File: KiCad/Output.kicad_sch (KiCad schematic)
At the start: 649 parts, among them J1 R_Phono_In, J10 VCC_IN, J11 VCC_OUT, J12 EMK_In, J15 Mic_Effekt_Out, J16 Mic_Effekt_Out, J17 Mic_Effekt_Out, J18 Mic_Effekt_Out, J19 Phono/Line_Out, J2 L_Phono_In, J20 Mic_Effekt_Out, J21 Conn_01x05_bridged, J22 Conn_02x07_Odd_Even, J24 Mic_Effekt_In, J25 Mic_Effekt_In, J26 Phono/Line_In, J27 Mic_Effekt_In, J28 Pegel_Out, J29 Pegel_Out, J3 R_Line_In, J30 Pegel_In, J31 Pegel_In, J32 Pegel_In, J33 Pegel_In, J34 LED_Out, J35 LED_In, J36 VU_Meter_Out, J37 AUX_Send_3, J38 AUX_Send_1, J39 AUX_Send_2, J4 L_Line_In, J40 Bass_Out, J41 Kick_Out, J42 Mid_Out, J43 High_Out, J44 Line_Out_L, J45 Line_Out_R, J5 Mic_In, J6 Effekt_In, J7 AUX_RET_1, J8 AUX_RET_2, J9 AUX_RET_3, SW1 SW_DPST, SW10 SW_SPDT, SW11 SW_SPDT, SW12 SW_SPDT, SW2 SW_SPDT, SW3 SW_SPDT, SW4 SW_SPDT, SW5 SW_SPDT, SW6 SW_SPDT, SW7 SW_SPDT, SW8 SW_SPDT, SW9 SW_Rotary_1x4, U1 TL074, U10 TL074, U11 TL074, U12 TL074, U13 TL074, U14 TL074, U15 TL074, U16 TL074, U17 TL074, U18 TL074, U19 TL074, U2 TL074, U20 TL074, U21 TL074, U22 TL074, U23 TL074, U24 TL074, U25 INA128U, U3 TL074, U4 TL074, U5 TL074, U6 REC10K-2409, U7 REC10K-2415, U8 TL074, U9 TL074

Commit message: final PCB Update
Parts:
- removed C114, C116, C117, C118, C7, C8: 100n, Capacitor_SMD:C_0805_2012Metric_Pad1.18x1.45mm_HandSolder, symbol Device:C_Small
- removed J12: EMK_In, Connector_PinHeader_2.54mm_LongPads:PinHeader_1x05_P2.54mm_Vertical_LongPads, symbol Connector:Conn_01x05_Pin
- removed J21: Conn_01x05_bridged, Connector_Bridged_2.54mm_LongPads:Bridge_2x05_P2.54mm_Vertical_LongPads, symbol conn_01x05_bridged:Conn_01x05_bridged
- removed R2: 100R, Resistor_SMD:R_0805_2012Metric_Pad1.20x1.40mm_HandSolder, symbol Device:R
- removed R25, R26, R27: 22R, Resistor_SMD:R_0805_2012Metric_Pad1.20x1.40mm_HandSolder, symbol Device:R
- removed unit 5 of U10
- removed unit 5 of U12
- removed unit 5 of U13
- removed unit 3 of U2
- removed U25: INA128U, INA128U:INA128U_L, symbol INA128U:INA128U
- removed unit 3 of U4
- added C114, C118, C91: 10u, Capacitor_THT:CP_Radial_D5.0mm_P2.50mm, symbol Device:C_Polarized_Small
- added C3: 10n, Capacitor_SMD:C_1210_3225Metric_Pad1.33x2.70mm_HandSolder, symbol Device:C_Small
- added C52, C53, C59, C60: 100n, Capacitor_SMD:C_0805_2012Metric_Pad1.18x1.45mm_HandSolder, symbol Device:C_Small
- added H1, H6, H7: MountingHole, MountingHole:MountingHole_3.2mm_M3_Pad, symbol Mechanical:MountingHole
- added H3: MountingHole_Pad, MountingHole:MountingHole_3.2mm_M3_Pad, symbol Mechanical:MountingHole_Pad
- added J30, J40, J41: Conn_02x07_Odd_Even, Connector_PinHeader_2.54mm:PinHeader_2x07_P2.54mm_Vertical, symbol Connector_Generic:Conn_02x07_Odd_Even
- added R52, R53, R57, R67, R75, R80: 10k, Resistor_SMD:R_0805_2012Metric_Pad1.20x1.40mm_HandSolder, symbol Device:R
- added unit 1 of U11
- added unit 3 of U11
- added unit 4 of U11
- added unit 2 of U11
- added unit 3 of U17
- added unit 5 of U18
- added unit 4 of U19
- added unit 5 of U2
- added unit 5 of U5
- added unit 5 of U7
- added unit 4 of U8
- added unit 2 of U8
- added unit 5 of U8
- added unit 3 of U8
- added unit 4 of U9
- added Z241, Z255, Z258: ~, Resistor_SMD:R_0805_2012Metric_Pad1.20x1.40mm_HandSolder, symbol Device:R
- RV11: renamed from RV3; footprint Connector_PinSocket_2.54mm_LongPads:PinSocket_1x06_P2.54mm_Vertical_LongPads -> Connector_PinSocket_2.54mm_LongPads:PinSocket_2x03_P2.54mm_Vertical_LongPads
- RV17: renamed from RV5; footprint Connector_PinSocket_2.54mm_LongPads:PinSocket_1x06_P2.54mm_Vertical_LongPads -> Connector_PinSocket_2.54mm_LongPads:PinSocket_2x03_P2.54mm_Vertical_LongPads_Mirrored
- U11: now not fitted; now left out of the parts list
- renumbered C21 to C1, C52 to C10, C112 to C100, C36 to C101, C24 to C102, C10 to C103, C67 to C104, C79 to C105, C97 to C106, C101 to C107, C105 to C108, C74 to C11, C11 to C110, C25 to C111, C4 to C112, C19 to C113, C2 to C115, C5 to C116, C20 to C117, C6 to C119, C43 to C12, C26 to C120, C12 to C121, C62 to C13, C86 to C14, C39 to C15, C49 to C16, C59 to C17, C71 to C18, C83 to C19, C27 to C2, C53 to C20, C75 to C21, C42 to C22, C63 to C23, C87 to C24, C38 to C25, C50 to C26, C60 to C27, C72 to C28, C84 to C29, C54 to C30, C76 to C31, C44 to C32, C3 to C33, C64 to C34, C88 to C35, C40 to C36, C1 to C37, C51 to C38, C61 to C39, C119 to C4, C73 to C40, C85 to C41, C55 to C42, C77 to C43, C45 to C44, C65 to C45, C89 to C46, C41 to C47, C30 to C48, C22 to C49, C48 to C5, C35 to C50, C37 to C51, C13 to C54, C16 to C55, C31 to C56, C33 to C57, C28 to C58, C58 to C6, C14 to C61, C17 to C62, C32 to C63, C34 to C64, C29 to C65, C110 to C66, C68 to C67, C80 to C68, C92 to C69, C70 to C7, C111 to C70, C69 to C71, C81 to C72, C93 to C73, C90 to C74, C94 to C75, C98 to C76, C102 to C77, C106 to C78, C91 to C79, C82 to C8, C95 to C80, C99 to C81, C103 to C82, C107 to C83, C9 to C84, C115 to C85, C23 to C86, C46 to C87, C56 to C88, C113 to C89, C15 to C9, C18 to C90, C47 to C92, C57 to C93, C66 to C94, C78 to C95, C100 to C97, C104 to C98, C108 to C99, D2 to D1, D1 to D2, D4 to D3, D3 to D4, H4 to H10, H8 to H11, H5 to H12, H2 to H13, H3 to H14, H6 to H15, H7 to H16, H12 to H2, H9 to H4, H11 to H5, H10 to H8, H1 to H9, J40 to J1, J42 to J10, J43 to J11, J20 to J12, J27 to J13, J16 to J14, J24 to J15, J15 to J16, J7 to J17, J38 to J18, J44 to J19, J1 to J2, J6 to J20, J45 to J21, J8 to J22, J17 to J23, J25 to J24, J37 to J25, J39 to J26, J18 to J27, J9 to J28, J28 to J29, J2 to J3, J22 to J31, J29 to J32, J30 to J33, J36 to J34, J31 to J35, J32 to J36, J34 to J37, J35 to J38, J10 to J39, J19 to J4, J33 to J42, J11 to J43, J26 to J5, J41 to J6, J3 to J7, J4 to J8, J5 to J9, L2 to L1, L3 to L2, L4 to L3, L1 to L4, R39 to R1, R117 to R10, R98 to R100, R23 to R101, R16 to R102, R19 to R103, R17 to R104, R21 to R105, R24 to R106, R43 to R107, R57 to R108, R145 to R109, R141 to R11, R33 to R110, R69 to R111, R76 to R112, R44 to R113, R121 to R114, R131 to R115, R79 to R116, R85 to R117, R99 to R118, R51 to R119, R93 to R12, R70 to R120, R100 to R121, R125 to R123, R45 to R124, R58 to R125, R9 to R126, R34 to R127, R46 to R128, R77 to R129, R40 to R13, R83 to R130, R123 to R131, R52 to R133, R10 to R134, R15 to R135, R78 to R136, R124 to R137, R80 to R138, R126 to R139, R49 to R14, R11 to R140, R67 to R141, R71 to R142, R81 to R143, R86 to R144, R59 to R145, R60 to R146, R68 to R147, R82 to R148, R84 to R149, R18 to R15, R72 to R150, R75 to R151, R6 to R16, R105 to R17, R113 to R18, R127 to R19, R55 to R2, R137 to R20, R146 to R21, R88 to R22, R94 to R23, R28 to R24, R32 to R25, R41 to R26, R56 to R27, R110 to R28, R134 to R29, R20 to R3, R14 to R30, R101 to R31, R29 to R32, R7 to R33, R118 to R34, R142 to R35, R31 to R36, R91 to R37, R42 to R38, R50 to R39, R22 to R4, R106 to R40, R114 to R41, R128 to R42, R138 to R43, R147 to R44, R8 to R45, R87 to R46, R92 to R47, R35 to R48, R53 to R49, R109 to R5, R111 to R50, R135 to R51, R61 to R54, R103 to R55, R36 to R56, R12 to R58, R119 to R59, R133 to R6, R143 to R60, R47 to R61, R73 to R63, R95 to R64, R3 to R65, R63 to R66, R107 to R68, R115 to R69, R13 to R7, R129 to R70, R139 to R71, R148 to R72, R89 to R73, R96 to R74, R1 to R76, R4 to R77, R37 to R78, R54 to R79, R102 to R8, R112 to R81, R136 to R82, R64 to R83, R104 to R84, R38 to R85, R120 to R86, R144 to R87, R48 to R88, R65 to R89, R5 to R9, R74 to R90, R97 to R91, R66 to R92, R30 to R93, R108 to R94, R116 to R95, R130 to R96, R140 to R97, R149 to R98, R90 to R99, RV9 to RV1, RV19 to RV10, RV14 to RV12, RV1 to RV13, RV8 to RV14, RV20 to RV15, RV15 to RV16, RV4 to RV18, RV16 to RV19, RV18 to RV2, RV21 to RV20, RV11 to RV21, RV13 to RV3, RV6 to RV4, RV10 to RV5, RV17 to RV6, RV12 to RV7, RV7 to RV8, RV2 to RV9, SW5 to SW1, SW12 to SW10, SW9 to SW11, SW1 to SW12, SW6 to SW3, SW3 to SW4, SW4 to SW5, SW7 to SW6, SW11 to SW7, SW10 to SW9, U8 to U1, U9 to U10, U16 to U12, U18 to U13, U13 to U14, U3 to U15, U17 to U16, U4 to U17, U5 to U17, U10 to U18, U5 to U19, U14 to U2, U21 to U20, U22 to U21, U20 to U22, U6 to U25, U7 to U26, U19 to U3, U1 to U4, U12 to U5, U15 to U6, U11 to U7, U4 to U8, U2 to U9, Z238 to Z1, Z68 to Z10, Z58 to Z100, Z214 to Z101, Z223 to Z102, Z187 to Z103, Z203 to Z104, Z232 to Z105, Z252 to Z106, Z156 to Z107, Z218 to Z108, Z19 to Z109, Z5 to Z11, Z195 to Z110, Z242 to Z111, Z9 to Z112, Z29 to Z113, Z243 to Z114, Z139 to Z115, Z151 to Z116, Z184 to Z117, Z201 to Z118, Z233 to Z119, Z25 to Z12, Z253 to Z120, Z145 to Z121, Z192 to Z122, Z160 to Z123, Z165 to Z124, Z162 to Z125, Z215 to Z126, Z224 to Z127, Z188 to Z128, Z204 to Z129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
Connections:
- net +15V_I: now also U11.4 (V+), C52.1, C53.2, J30.13 (Pin_13), J30.14 (Pin_14), U8.4 (V+)
- net +15V_M: now also J41.13 (Pin_13), J41.14 (Pin_14)
- net +15V_O: now also U18.4 (V+), U2.4 (V+), U5.4 (V+), U7.4 (V+); no longer U11.4 (V+)
- net +15V_P: now also C114.1, J40.13 (Pin_13), J40.14 (Pin_14), Z255.2
- net +9V_I: now also J30.5 (Pin_5), J30.6 (Pin_6)
- net +9V_M: now also J41.5 (Pin_5), J41.6 (Pin_6)
- net +9V_P: now also C91.1, J40.5 (Pin_5), J40.6 (Pin_6), Z241.2
- net -15V_I: now also U11.11 (V-), C59.2, C60.2, J30.7 (Pin_7), J30.8 (Pin_8), U8.11 (V-)
- net -15V_M: now also J41.7 (Pin_7), J41.8 (Pin_8)
- net -15V_O: now also U18.11 (V-), U2.11 (V-), U5.11 (V-), U7.11 (V-); no longer U11.11 (V-)
- net -15V_P: now also C118.2, J40.7 (Pin_7), J40.8 (Pin_8), Z258.2
- net 9V_GND_I: now also J30.1 (Pin_1), J30.2 (Pin_2), J30.3 (Pin_3), J30.4 (Pin_4)
- net 9V_GND_M: now also J41.1 (Pin_1), J41.2 (Pin_2), J41.3 (Pin_3), J41.4 (Pin_4)
- net 9V_GND_P: now also C91.2, J40.1 (Pin_1), J40.2 (Pin_2), J40.3 (Pin_3), J40.4 (Pin_4)
- net GND_I: now also J9.2 (Pin_2), Z143.1, C3.2, C52.2, C53.1, C59.1, C60.1, J30.10 (Pin_10), J30.11 (Pin_11), J30.12 (Pin_12), J30.9 (Pin_9), R80.1, U11.12 (+), U8.12 (+), U9.12 (+); no longer J9.1 (Pin_1), Z143.2
- net GND_M: now also J41.10 (Pin_10), J41.11 (Pin_11), J41.12 (Pin_12), J41.9 (Pin_9)
- net GND_P: now also C114.2, C118.1, J40.10 (Pin_10), J40.11 (Pin_11), J40.12 (Pin_12), J40.9 (Pin_9)
- net at RV9.1: now also R67.2, U11.2 (-)
- net at RV9.2, RV9.3: now also R57.1, U11.6 (-)
- net at R135.1, Z204.1, Z211.1: now also U19.8; no longer U19.7
- net at R126.1, R134.1, R135.2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: now also U19.9 (-); no longer U19.6 (-)
- net at R32.1, RV4.2, RV4.3: now also U8.6 (-)
- net at R32.2, R36.2: now also U8.10 (+); no longer U15.5 (+)
- net at Z189.2, Z193.1: now also U17.3 (+); no longer U17.12 (+)
- net at C117.2, C120.1, C121.2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: now also Z258.1
- net at C110.2, C111.2, C113.1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: now also Z255.1
- net at Z201.2, Z207.1: now also U19.3 (+); no longer U19.12 (+)
- net at R102.2, R103.1, R104.2: now also U17.13 (-); no longer U17.6 (-)
- net at R103.2, Z136.1: now also U17.14; no longer U17.7
- net at Z109.1, Z112.1: now also J9.1 (Pin_1); no longer J9.3 (Pin_3)
- net at R25.2, Z38.1, Z40.1: now also U8.8; no longer U15.7
- net at Z80.2, Z87.1: now also U11.5 (+)
- net at R102.1: now also Z135.2; no longer Z98.2
- net at Z109.2, Z113.1: now also U11.3 (+)
- net at Z80.1, Z86.1: now also J9.3 (Pin_3); no longer J9.2 (Pin_2)
- net at R65.1, RV13.1: now also Z95.2; no longer Z135.2
- net at RV13.2: now also U15.5 (+); no longer U15.10 (+)
- net at R58.2, RV13.3, Z97.1: now also U15.8
- net at Z176.2, Z181.1: now also U17.5 (+); no longer U17.3 (+)
- net at C84.2, C86.2, C90.1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: now also Z241.1
- net at Z151.1: now also U17.12 (+); no longer U17.5 (+)
- net at Z224.1: now also U19.10 (+); no longer U19.5 (+)
- net at R24.1, RV4.1: now also U8.7
- net at R101.1, RV18.1: now also Z98.2; no longer Z95.2
- net at C33.1, RV11.1, RV11.2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: now also U15.10 (+)
- net at R58.1, R65.2: now also U15.9 (-)
- net at Z94.1: now also R53.1, U11.8
- net at Z225.2, Z230.1: now also U19.5 (+); no longer U19.10 (+)
- net at Z63.1: now also U9.10 (+); no longer U9.12 (+)
- net at R30.1, R33.2, R45.2: now also U9.9 (-); no longer U9.13 (-)
- net at R30.2, Z54.1: now also U9.8; no longer U9.14
- net at SW2.2 (B): now also U8.5 (+)
- net at Z134.2, Z135.1: now also Z143.2; no longer Z143.1
- net at R24.2, R25.1: now also U8.9 (-); no longer U15.6 (-)
- new net: U19.1, U19.2 (-), Z202.1
- new net: R67.1, R75.1, U11.1
- new net: R75.2, R80.2, U11.10 (+)
- new net: U17.1, U17.2 (-), Z190.1
- new net: U17.10 (+), U19.12 (+), U8.3 (+), Z137.2
- new net: U9.13 (-), U9.14
- new net: U8.13 (-), U8.14
- new net: C37.2, U15.6 (-), U15.7
- new net: U19.13 (-), U19.14, Z152.1, Z156.1
- new net: U17.6 (-), U17.7, Z155.2
- new net: U17.8, U17.9 (-), Z175.1, Z177.1
- new net: R52.2, R53.2, U11.9 (-)
- new net: U11.13 (-), U11.14
- new net: C3.1, H3.1
- new net: R52.1, R57.2, U11.7
- new net: U19.6 (-), U19.7, Z226.1
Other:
- moved on the sheet: C1, C10, C100, C101, C102, C103, C104, C105, C106, C107, C108, C109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

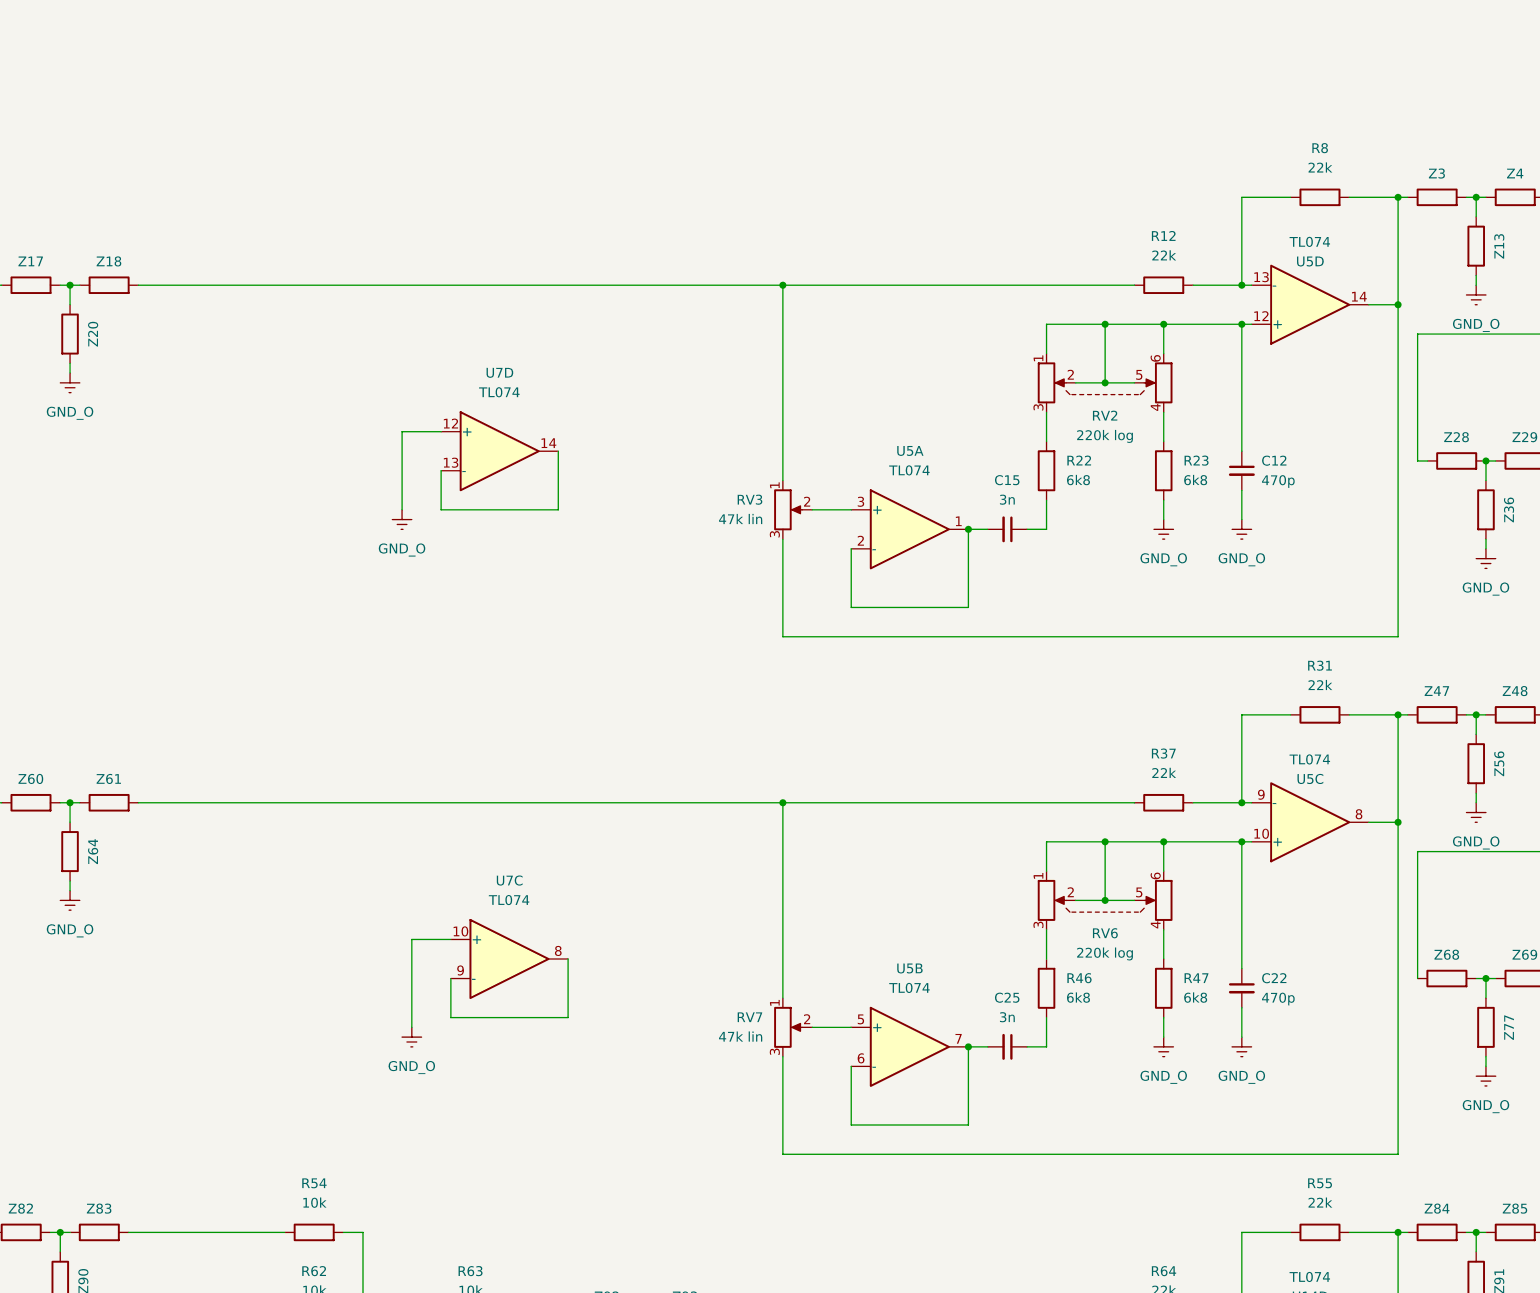
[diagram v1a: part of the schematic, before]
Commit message: Output phasen korrektur durch invertierender verstärker
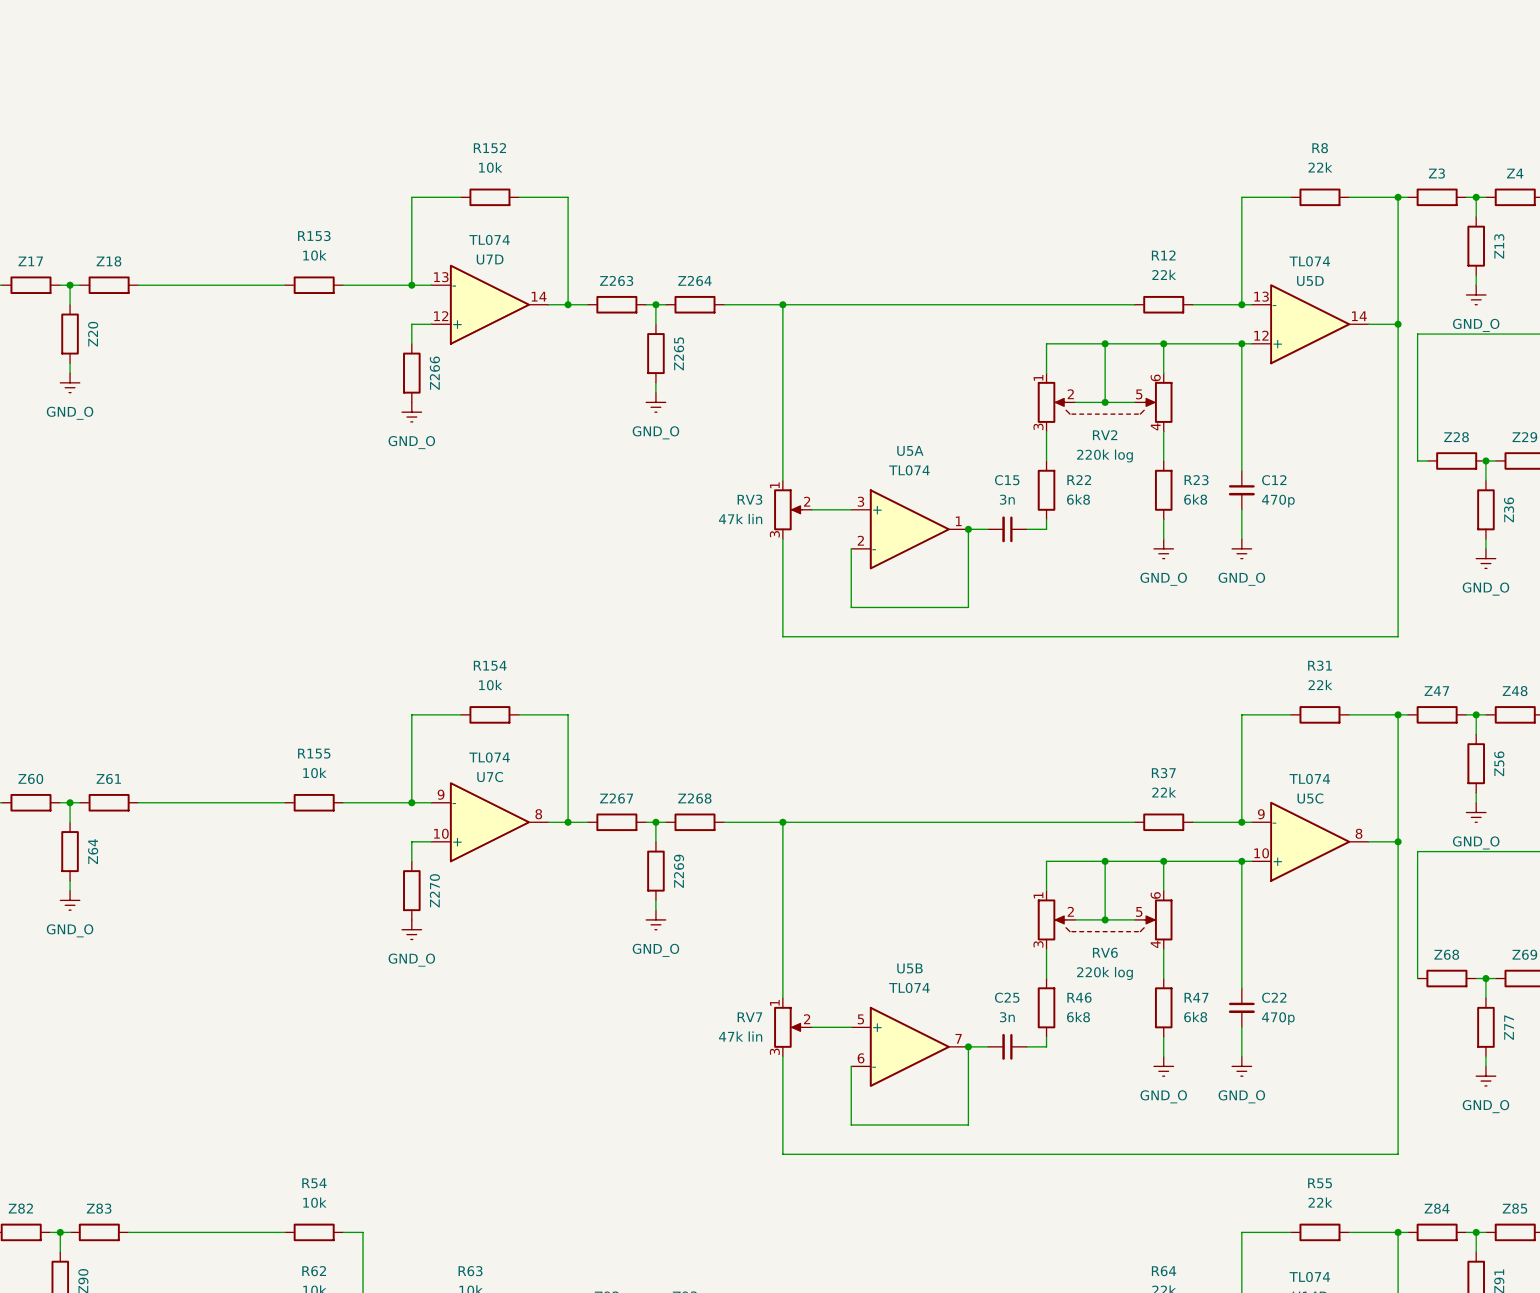
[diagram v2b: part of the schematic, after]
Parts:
- added R152, R153, R154, R155: 10k, Resistor_SMD:R_0805_2012Metric_Pad1.20x1.40mm_HandSolder, symbol Device:R
- added Z263, Z264, Z265, Z266, Z267, Z268, Z269, Z270: ~, Resistor_SMD:R_0805_2012Metric_Pad1.20x1.40mm_HandSolder, symbol Device:R
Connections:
- net GND_O: now also Z265.2, Z266.2, Z269.2, Z270.2; no longer U7.10 (+), U7.12 (+)
- net at R37.1, RV7.1: now also Z268.2; no longer Z61.2
- net at U7.13 (-): now also R152.1, R153.2; no longer U7.14
- net at R12.1, RV3.1: now also Z264.2; no longer Z18.2
- net at U7.9 (-): now also R154.1, R155.2; no longer U7.8
- new net: R155.1, Z61.2
- new net: Z267.2, Z268.1, Z269.1
- new net: U7.12 (+), Z266.1
- new net: R152.2, U7.14, Z263.1
- new net: U7.10 (+), Z270.1
- new net: R154.2, U7.8, Z267.1
- new net: R153.1, Z18.2
- new net: Z263.2, Z264.1, Z265.1
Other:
- moved on the sheet: C12, C22, R12, R22, R23, R37, R46, R47, RV2, RV6, U5C, U5D

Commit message: Output Stage in phase gebracht
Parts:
- added R156, R157: 10k, Resistor_SMD:R_0805_2012Metric_Pad1.20x1.40mm_HandSolder, symbol Device:R
- added Z271, Z272, Z273, Z274: ~, Resistor_SMD:R_0805_2012Metric_Pad1.20x1.40mm_HandSolder, symbol Device:R
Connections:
- net GND_O: now also Z271.2, Z274.2; no longer U20.5 (+)
- net at U20.12 (+), U20.3 (+), Z231.2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: now also Z273.2; no longer Z174.2
- net at U20.7: now also R156.2, Z272.1; no longer U20.6 (-)
- new net: U20.5 (+), Z271.1
- new net: R157.1, Z174.2
- new net: Z272.2, Z273.1, Z274.1
- new net: R156.1, R157.2, U20.6 (-)
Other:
- moved on the sheet: C104, C105, C106, C107, C108, C109, C66, C67, C68, C69, C70, C71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

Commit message: final pcb update
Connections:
- net at U20.8, Z166.1: now also R109.2; no longer R109.1
- net at R21.2, R44.2, R72.2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: now also R109.1; no longer R109.2
- net at U20.7, Z272.1: now also R156.1; no longer R156.2
- net at R157.2, U20.6 (-): now also R156.2; no longer R156.1
- net at R116.2, RV19.1, RV19.2: no longer R117.2, RV19.5, RV19.6
- new net: R117.2, RV19.5, RV19.6
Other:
- moved on the sheet: J19, J21, R109, R156, R157, U20A, U20B, U20C, U20D, Z166, Z172, Z173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

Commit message: Update mit Fotos und Blockschaltbild
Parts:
- added R158, R159: 10k, Resistor_SMD:R_0805_2012Metric_Pad1.20x1.40mm_HandSolder, symbol Device:R
- L4, Z1, Z10, Z100, Z101, Z102, Z103, Z104, Z105, Z106, Z107, Z108, Z109, Z11, Z110, Z111, Z112, Z113, Z114, Z115, Z116, Z117, Z118, Z119, Z12, Z120, Z121, Z122, Z123, Z124, Z125, Z126, Z127, Z128, Z129, Z13, Z130, Z131, Z132, Z133, Z134, Z135, Z136, Z137, Z138, Z139, Z14, Z140, Z141, Z142, Z143, Z144, Z145, Z146, Z147, Z148, Z149, Z15, Z150, Z151, Z152, Z153, Z154, Z155, Z156, Z157, Z158, Z159, Z16, Z160, Z161, Z162, Z163, Z164, Z165, Z166, Z167, Z168, Z169, Z17, Z170, Z171, Z172, Z173, Z174, Z175, Z176, Z177, Z178, Z179, Z18, Z180, Z181, Z182, Z183, Z184, Z185, Z186, Z187, Z188, Z189, Z19, Z190, Z191, Z192, Z193, Z194, Z195, Z196, Z197, Z198, Z199, Z2, Z20, Z200, Z201, Z202, Z203, Z204, Z205, Z206, Z207, Z208, Z209, Z21, Z210, Z211, Z212, Z213, Z214, Z215, Z216, Z217, Z218, Z219, Z22, Z220, Z221, Z222, Z223, Z224, Z225, Z226, Z227, Z228, Z229, Z23, Z230, Z231, Z232, Z233, Z234, Z235, Z236, Z237, Z238, Z239, Z24, Z240, Z241, Z242, Z243, Z244, Z245, Z246, Z247, Z248, Z249, Z25, Z250, Z251, Z252, Z253, Z254, Z255, Z256, Z257, Z258, Z259, Z26, Z260, Z261, Z262, Z263, Z264, Z265, Z266, Z267, Z268, Z269, Z27, Z270, Z271, Z272, Z273, Z274, Z28, Z29, Z3, Z30, Z31, Z32, Z33, Z34, Z35, Z36, Z37, Z38, Z39, Z4, Z40, Z41, Z42, Z43, Z44, Z45, Z46, Z47, Z48, Z49, Z5, Z50, Z51, Z52, Z53, Z54, Z55, Z56, Z57, Z58, Z59, Z6, Z60, Z61, Z62, Z63, Z64, Z65, Z66, Z67, Z68, Z69, Z7, Z70, Z71, Z72, Z73, Z74, Z75, Z76, Z77, Z78, Z79, Z8, Z80, Z81, Z82, Z83, Z84, Z85, Z86, Z87, Z88, Z89, Z9, Z90, Z91, Z92, Z93, Z94, Z95, Z96, Z97, Z98, Z99: value ~ -> (none)
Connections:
- net at R66.1, R92.1, Z205.2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: now also R159.1
- net at R154.1, R155.2, U7.9 (-): now also R158.2, R159.2
- net at R62.1, R89.1, Z141.2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: now also R158.1
